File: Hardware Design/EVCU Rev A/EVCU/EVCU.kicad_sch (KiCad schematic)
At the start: 78 parts, among them J1 Conn_01x06, J10 Conn_01x10_Female, J2 Conn_01x02, J3 APPS/BSE_Conn, J4 Micro_SD_Card, J5 DB9_Male, J6 Conn_01x02, J7 Conn_01x10_Female, J8 Conn_01x10_Female, J9 Conn_01x10_Female, U1 AZ1084-3.3, U10 EMIF06-MSD02N16, U11 ESDALC6V1W5, U2 AP62250WU-7, U3 STM32L4R9ZITx, U4 LM358, U5 MPU-6500, U6 SN65HVD230, U7 LM358, U8 LM358, U9 ESDCAN24-2BLY, X1 ECS-2520MV-160-CN-TR

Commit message: should be done.
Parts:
- removed J10, J7, J8, J9: Conn_01x10_Female, Connector_PinSocket_2.54mm:PinSocket_1x10_P2.54mm_Vertical, symbol Connector:Conn_01x10_Female
- removed U1: AZ1084-3.3, Package_TO_SOT_SMD:TO-252-3_TabPin2, symbol Regulator_Linear:AZ1084-3.3
- added JP1, JP2, JP3: SolderJumper_3_Open, Jumper:SolderJumper-3_P1.3mm_Open_Pad1.0x1.5mm_NumberLabels, symbol Jumper:SolderJumper_3_Open
- added TP1, TP2, TP3, TP4, TP5, TP6, TP7: TestPoint_Probe, TestPoint:TestPoint_Pad_1.5x1.5mm, symbol Connector:TestPoint_Probe
- added U1: AMS1117-3.3, Package_TO_SOT_SMD:SOT-223-3_TabPin2, symbol Regulator_Linear:AMS1117-3.3
- C3: Rating 25V -> 50V
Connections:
- net +3V3: now also U3.108 (VDDUSB), TP1.1, U1.2 (VO)
- net +5V: now also TP2.1, U1.3 (VI)
- net +BATT: now also U2.5 (EN)
- net CAN_H: now also TP3.1
- net CAN_L: now also TP4.1
- net GND: now also U1.1 (GND)
- net VOUT_1_APPS: now also JP1.1 (A); no longer C25.1, R8.1
- net VOUT_2_APPS: now also JP2.1 (A); no longer C26.1, R9.1
- net VOUT_BSE: now also JP3.1 (A); no longer C30.1, R4.1
- new net: C25.1, JP1.2 (C), R8.1
- new net: JP1.3 (B), TP5.1
- new net: C30.1, JP3.2 (C), R4.1
- new net: C26.1, JP2.2 (C), R9.1
- new net: JP3.3 (B), TP7.1
- new net: JP2.3 (B), TP6.1
- no-connect marks 104 -> 102
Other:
- note removed: "Debug Pins (NEED TO BE FIGURED OUT)"
- moved on the sheet: C20, C21, C29, D1, J1, J4, R1, U10, U11, U3, X1

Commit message: cap 1206 change, fuse, lin reg to 1117, testpoints, bom additions
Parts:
- removed F1: Fuse, Fuse:Fuse_0805_2012Metric_Pad1.15x1.40mm_HandSolder, symbol Device:Fuse
- removed U1: AMS1117-3.3, Package_TO_SOT_SMD:SOT-223-3_TabPin2, symbol Regulator_Linear:AMS1117-3.3
- added F1: 3557-2, 3557-2:3557-2, symbol Device:3557-2
- added U1: AZ1117-3.3, Package_TO_SOT_SMD:SOT-89-3_Handsoldering, symbol Regulator_Linear:AZ1117-3.3
- C3: footprint Capacitor_SMD:C_0603_1608Metric_Pad1.08x0.95mm_HandSolder -> Capacitor_SMD:C_1206_3216Metric_Pad1.33x1.80mm_HandSolder
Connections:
- net +3V3: now also U1.2 (VO)
- net +5V: now also J3.1 (Pin_1), U1.3 (VI); no longer J3.2 (Pin_2)
- net +BATT: now also F1. (4)
- net GND: now also J3.3 (Pin_3), U1.1 (GND)
- net VPA_BSE: now also J3.2 (Pin_2); no longer J3.1 (Pin_1)
- net at J2.1 (Pin_1): now also F1. (4)
- no-connect marks 102 -> 101
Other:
- moved on the sheet: C20, C21, D1, J1, J2, R1, TP1, TP2, U11, U3, X1

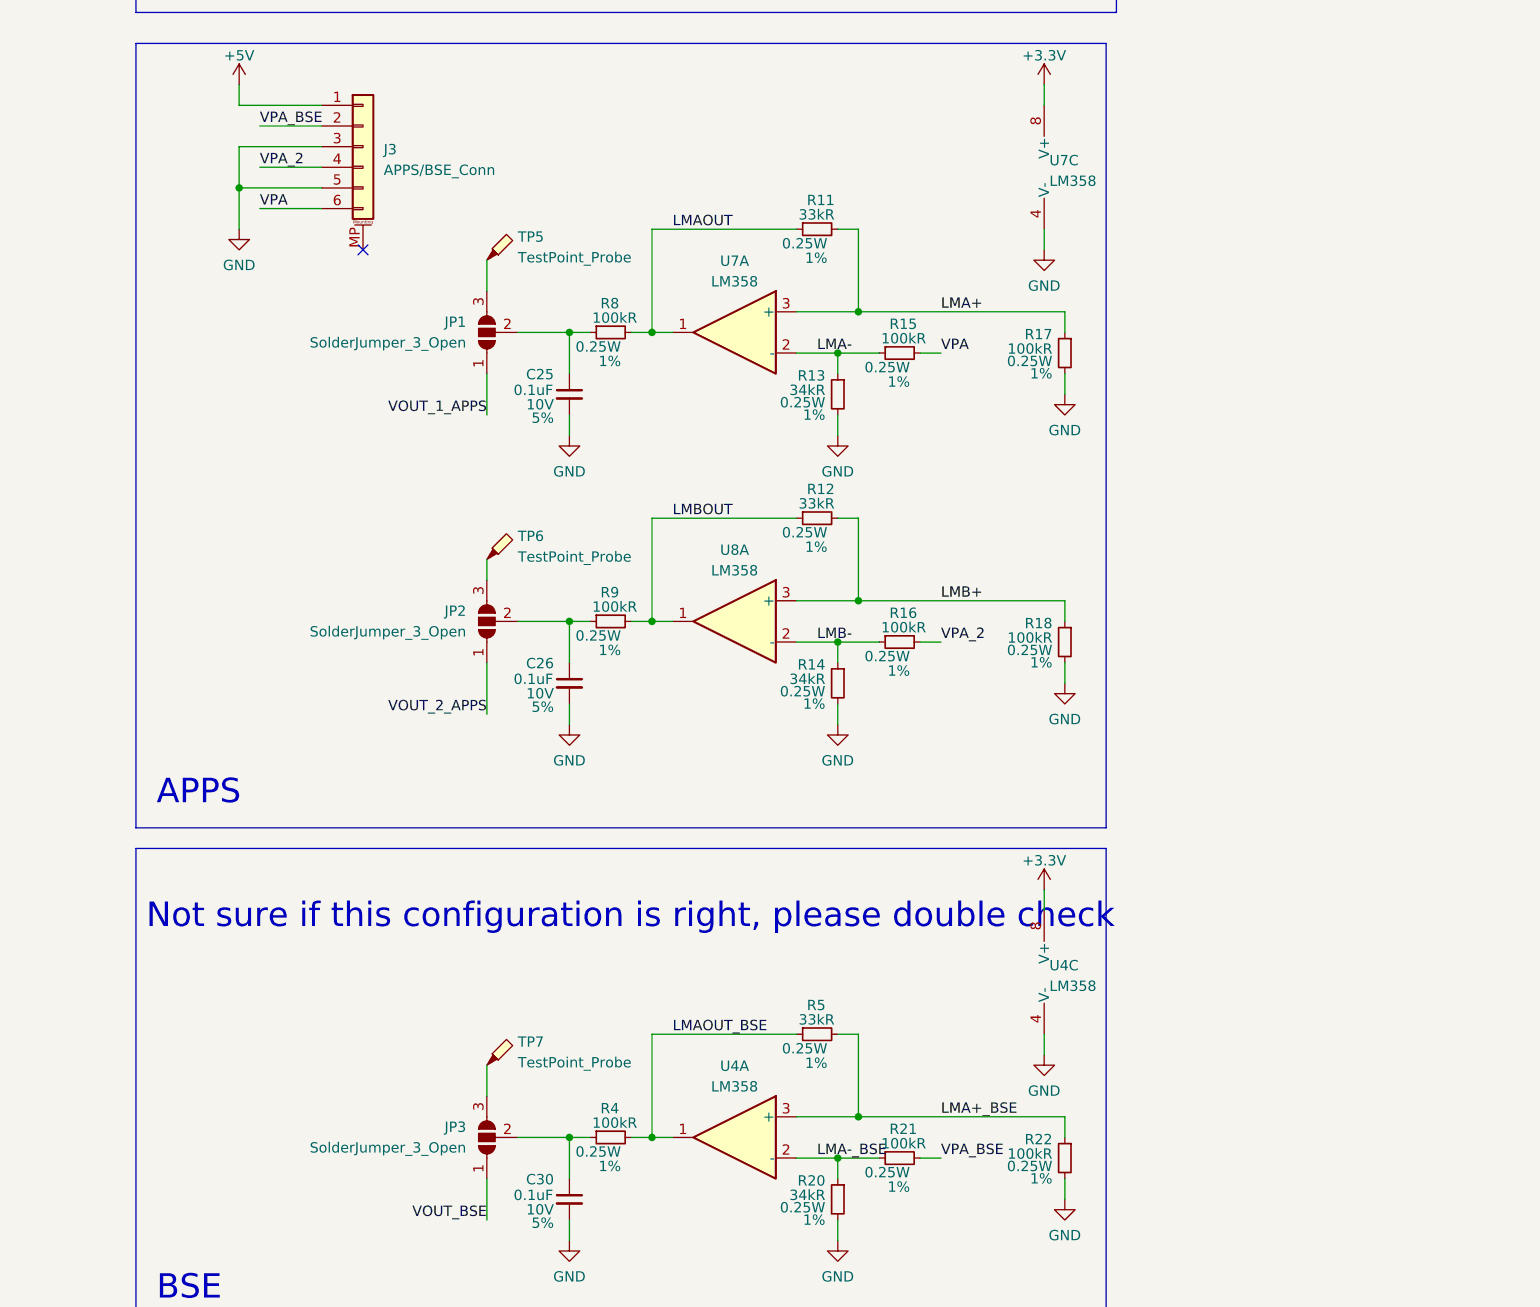
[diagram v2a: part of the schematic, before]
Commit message: accelerometer layout and op-amp footprint
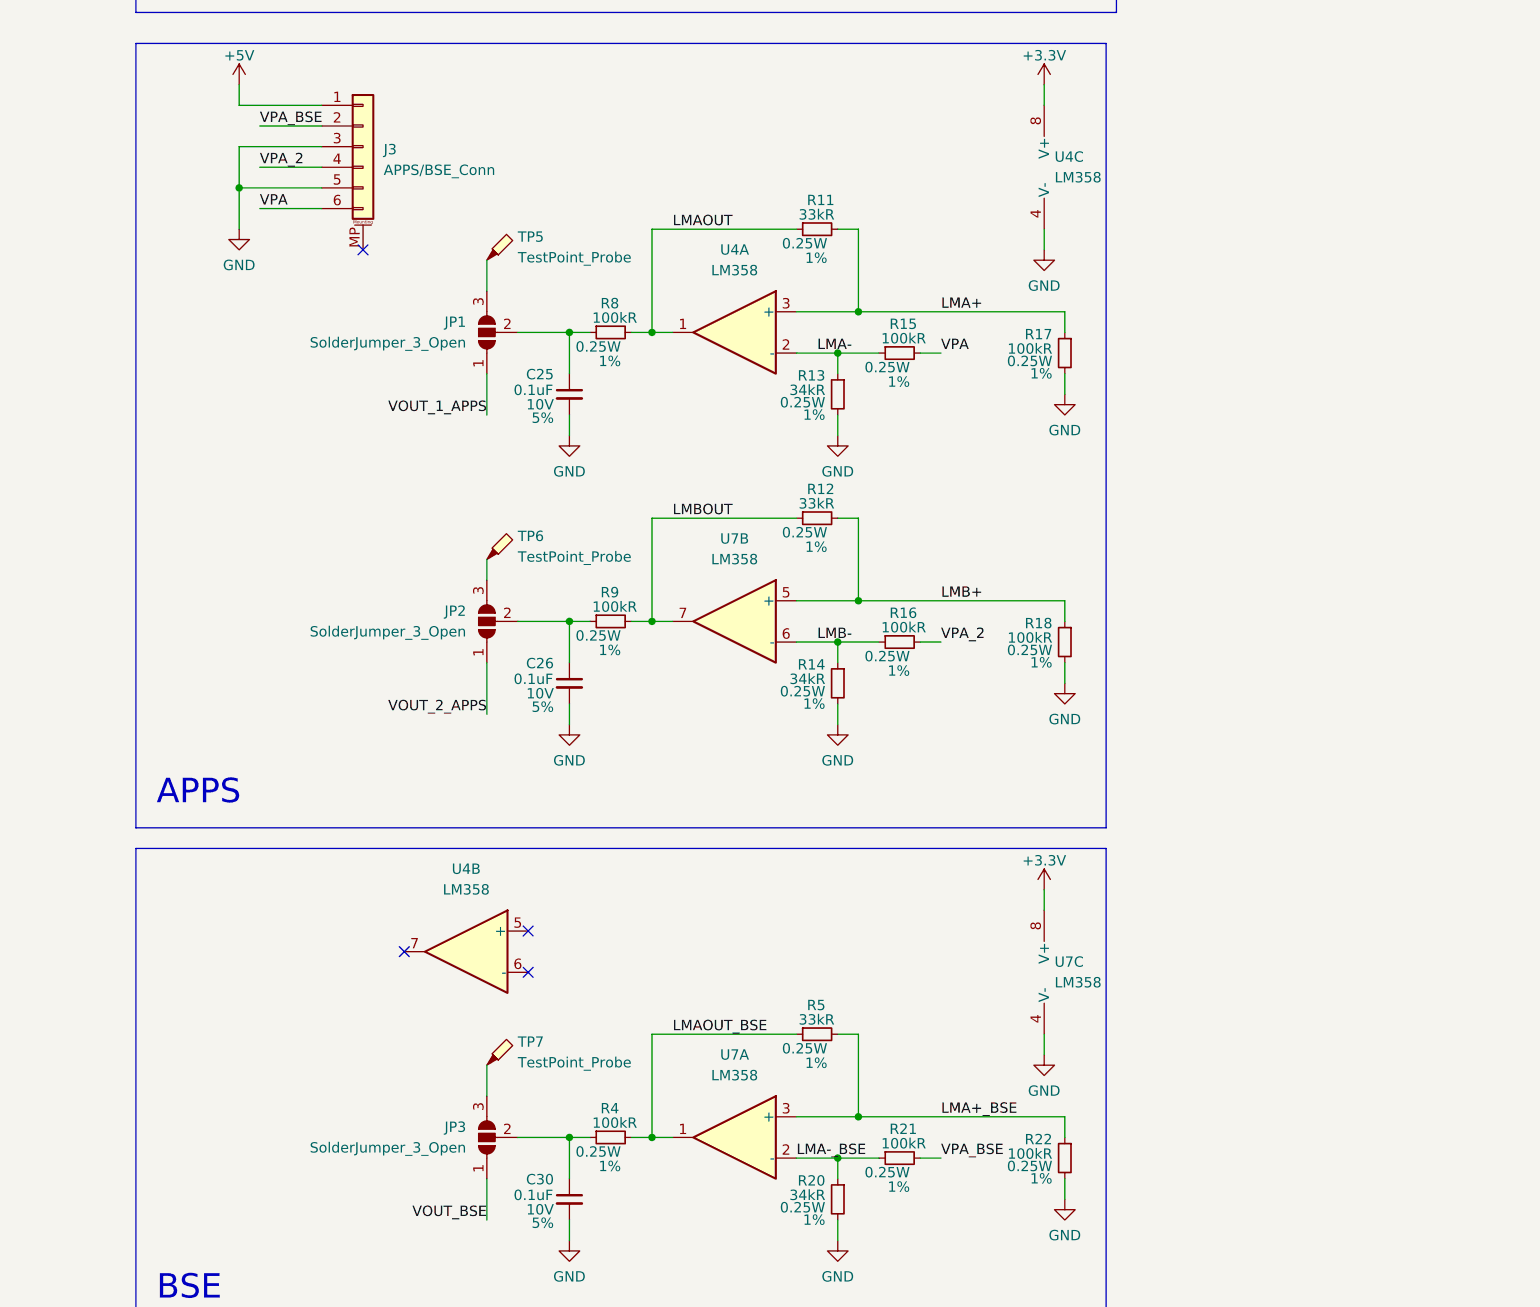
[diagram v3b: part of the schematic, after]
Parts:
- removed U8: LM358, symbol Amplifier_Operational:LM358
- added unit 2 of U4
- added unit 2 of U7
- U4, U7: footprint (none) -> Package_SO:SOIC-8-1EP_3.9x4.9mm_P1.27mm_EP2.29x3mm
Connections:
- net LMA+: now also U4.3 (+); no longer U7.3 (+)
- net LMA+_BSE: now also U7.3 (+); no longer U4.3 (+)
- net LMA-: now also U4.2 (-); no longer U7.2 (-)
- net LMA-_BSE: now also U7.2 (-); no longer U4.2 (-)
- net LMAOUT: now also U4.1; no longer U7.1
- net LMAOUT_BSE: now also U7.1; no longer U4.1
- net LMB+: now also U7.5 (+)
- net LMB-: now also U7.6 (-)
- net LMBOUT: now also U7.7
- no-connect marks 101 -> 104
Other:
- note removed: "Not sure if this configuration is right, please double check"

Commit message: dcdc and filter layout
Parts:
- R2: footprint Inductor_SMD:L_0805_2012Metric_Pad1.05x1.20mm_HandSolder -> Resistor_SMD:R_0805_2012Metric_Pad1.20x1.40mm_HandSolder
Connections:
- net LMB+: now also U4.5 (+); no longer U7.5 (+)
- net LMB-: now also U4.6 (-); no longer U7.6 (-)
- net LMBOUT: now also U4.7; no longer U7.7
- net FB: now reaches R2.2, R3.1, U2.4 (FB)
- net SW: now reaches C22.2, L2.1, U2.2 (SW)
- net BST: now reaches C22.1, U2.6 (BST)

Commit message: PCB layout for 1st iteration done, some labelling required
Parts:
- added C31: 100nF, Capacitor_SMD:C_0603_1608Metric_Pad1.08x0.95mm_HandSolder, symbol Device:C_Small
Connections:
- net +3V3: now also C31.1
- net GND: now also C31.2
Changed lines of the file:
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@@
   (junction (at 294.64 264.16) (diameter 0) (color 0 0 0 0)
   )
+  (junction (at 109.22 22.86) (diameter 0) (color 0 0 0 0)
+  )
   (junction (at 363.22 106.68) (diameter 0) (color 0 0 0 0)
   )
@@
   (junction (at 274.32 264.16) (diameter 0) (color 0 0 0 0)
   )
+  (junction (at 109.22 33.02) (diameter 0) (color 0 0 0 0)
+  )
   (junction (at 83.82 116.84) (diameter 0) (color 0 0 0 0)
   )
@@
     (stroke (width 0) (type default) (color 0 0 0 0))
   )
-  (polyline (pts (xy 119.38 12.7) (xy 119.38 76.2))
+  (polyline (pts (xy 129.54 12.7) (xy 129.54 76.2))
     (stroke (width 0) (type default) (color 0 0 0 0))
   )
@@
     (stroke (width 0) (type default) (color 0 0 0 0))
   )
-  (polyline (pts (xy 17.78 12.7) (xy 119.38 12.7))
+  (polyline (pts (xy 17.78 12.7) (xy 129.54 12.7))
     (stroke (width 0) (type default) (color 0 0 0 0))
   )
@@
     (stroke (width 0) (type default) (color 0 0 0 0))
   )
+  (wire (pts (xy 109.22 33.02) (xy 119.38 33.02))
+    (stroke (width 0) (type default) (color 0 0 0 0))
+  )
   (wire (pts (xy 55.88 58.42) (xy 55.88 60.96))
     (stroke (width 0) (type default) (color 0 0 0 0))
@@
     (stroke (width 0) (type default) (color 0 0 0 0))
   )
+  (wire (pts (xy 109.22 22.86) (xy 119.38 22.86))
+    (stroke (width 0) (type default) (color 0 0 0 0))
+  )
   (wire (pts (xy 274.32 78.74) (xy 274.32 81.28))
     (stroke (width 0) (type default) (color 0 0 0 0))
@@
     (stroke (width 0) (type default) (color 0 0 0 0))
   )
+  (wire (pts (xy 119.38 22.86) (xy 119.38 25.4))
+    (stroke (width 0) (type default) (color 0 0 0 0))
+  )
   (wire (pts (xy 299.72 78.74) (xy 302.26 78.74))
     (stroke (width 0) (type default) (color 0 0 0 0))
@@
     (stroke (width 0) (type default) (color 0 0 0 0))
   )
-  (polyline (pts (xy 119.38 76.2) (xy 12.7 76.2))
+  (polyline (pts (xy 129.54 76.2) (xy 12.7 76.2))
     (stroke (width 0) (type default) (color 0 0 0 0))
   )
@@
     (stroke (width 0) (type default) (color 0 0 0 0))
   )
+  (wire (pts (xy 119.38 30.48) (xy 119.38 33.02))
+    (stroke (width 0) (type default) (color 0 0 0 0))
+  )
   (wire (pts (xy 226.06 99.06) (xy 226.06 96.52))
     (stroke (width 0) (type default) (color 0 0 0 0))
@@
     (pin "9")
   )
+  (symbol (lib_id "Device:C_Small") (at 119.38 27.94 0) (unit 1)
+    (in_bom yes) (on_board yes)
+    (property "Reference" "C31" (id 0) (at 121.285 25.5 0)
+      (effects (font (size 1.27 1.27)) (justify left))
+    )
+    (property "Value" "100nF" (id 1) (at 121.375 27.432 0)
+      (effects (font (size 1.27 1.27)) (justify left))
+    )
+    (property "Footprint" "Capacitor_SMD:C_0603_1608Metric_Pad1.08x0.95mm_HandSolder" (id 2) (at 119.38 27.94 0)
+      (effects (font (size 1 1)) hide)
+    )
+    (property "Datasheet" "~" (id 3) (at 119.38 27.94 0)
+      (effects (font (size 1 1)) hide)
+    )
+    (property "Rating" "10V" (id 4) (at 121.285 29.21 0)
+      (effects (font (size 1.27 1.27)) (justify left))
+    )
+    (property "Tolerance" "5%" (id 5) (at 121.285 30.861 0)
+      (effects (font (size 1.27 1.27)) (justify left))
+    )
+    (pin "1")
+    (pin "2")
+  )
   (symbol (lib_id "Device:C_Small") (at 58.42 27.94 0) (unit 1)
     (in_bom yes) (on_board yes)
@@
       (reference "C30") (unit 1) (value "0.1uF") (footprint "Capacitor_SMD:C_0603_1608Metric_Pad1.08x0.95mm_HandSolder")
     )
+    (path "/d4ec61da-c2f6-4981-a76c-b66ff545de31"
+      (reference "C31") (unit 1) (value "100nF") (footprint "Capacitor_SMD:C_0603_1608Metric_Pad1.08x0.95mm_HandSolder")
+    )
     (path "/1ebdb596-e85b-47a1-8722-877bf4da7f08"

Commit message: layout
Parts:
- added H1, H2, H3, H4: MountingHole, MountingHole:MountingHole_2.1mm, symbol Mechanical:MountingHole
- added J7, J8, J9, J? (x6): Conn_01x10, Connector_PinSocket_2.54mm:PinSocket_1x10_P2.54mm_Vertical, symbol Connector_Generic:Conn_01x10
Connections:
- new net: J?.1 (Pin_1), J?.10 (Pin_10)
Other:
- note added: "Mounting Holes"
- note added: "Pin Sockets"

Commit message: ur mom
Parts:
- removed J7, J8, J9, J? (x6): Conn_01x10, Connector_PinSocket_2.54mm:PinSocket_1x10_P2.54mm_Vertical, symbol Connector_Generic:Conn_01x10
- added Q1: Q_PMOS_GSD, Package_TO_SOT_SMD:SOT-23, symbol Device:Q_PMOS_GSD
- U5: footprint Package_DFN_QFN:QFN-24-1EP_3x3mm_P0.4mm_EP1.75x1.6mm_ThermalVias -> Package_DFN_QFN:QFN-24-3x3mm_P0.4mm_EP1.75x1.6mm
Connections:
- net GND: now also Q1.1 (G)
- net at J2.1 (Pin_1): now also Q1.2 (S); no longer F1. (4)
- new net: F1. (4), Q1.3 (D)
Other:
- note removed: "Pin Sockets"
- moved on the sheet: F1, J2
